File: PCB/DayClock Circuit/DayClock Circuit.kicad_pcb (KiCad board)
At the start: 2 copper layers, 30 x 75 mm, 11 parts, among them J1 Servo Conn_01x03_Male, J2 LED Strip Conn_01x03_Male, J3 5V Power Connector, J4 Input Button Connector, U1 Tiny_RTC_DS1307

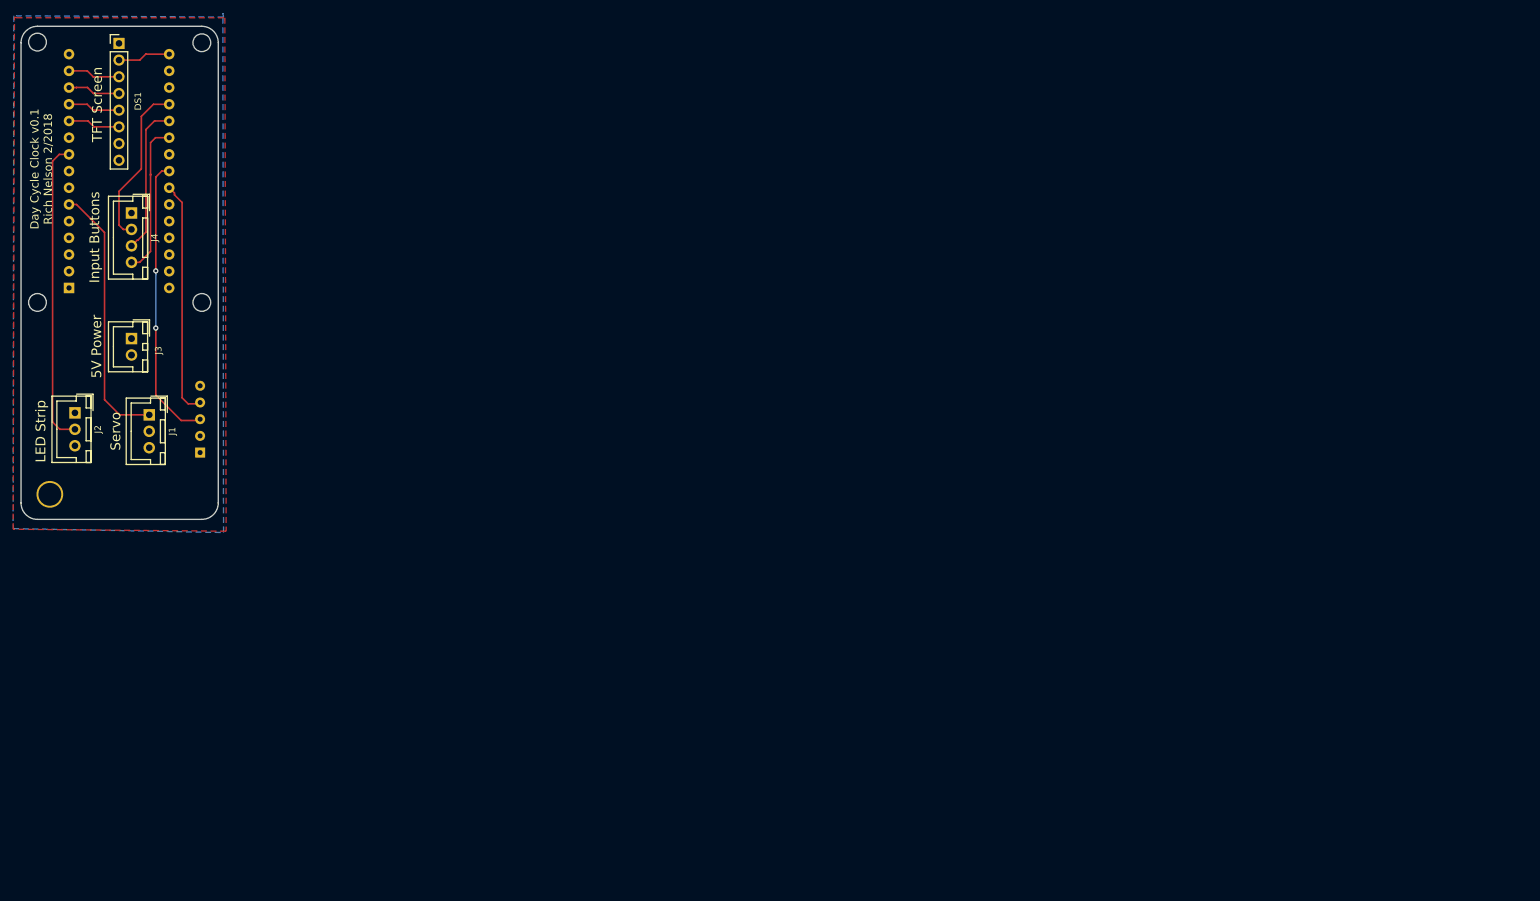
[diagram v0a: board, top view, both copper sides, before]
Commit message: Started moving components to the Arduino Mega,  moved the 3 LED strips (9 PWM pins), and the 32x64 Matrix Display
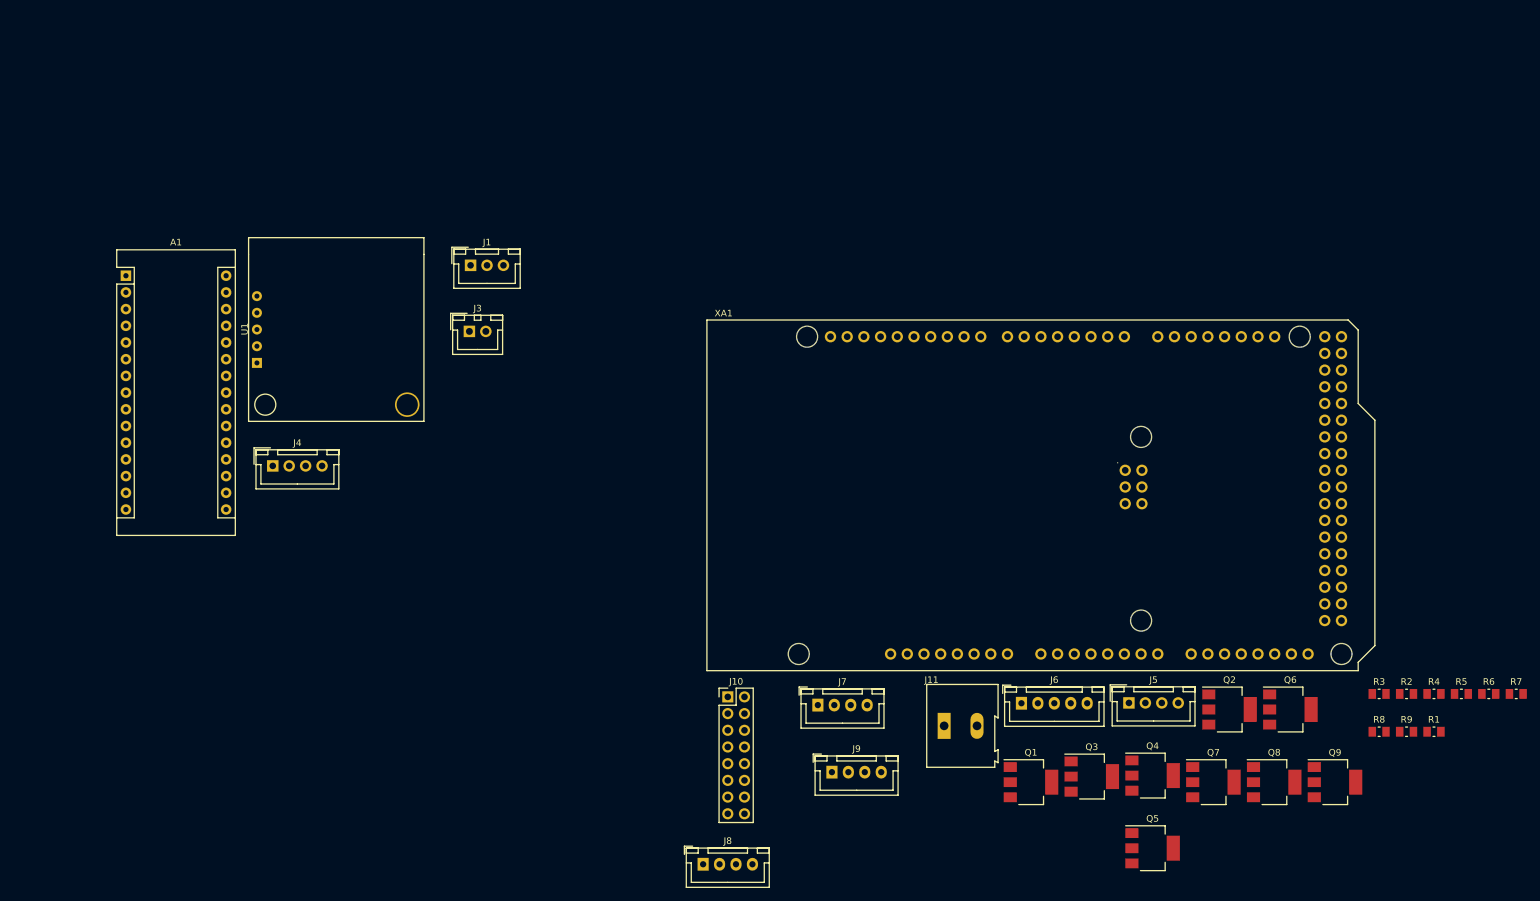
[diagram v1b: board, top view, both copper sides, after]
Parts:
- removed DS1: TFT-Screen-1.44-SPI-128*128, Socket_Strips:Socket_Strip_Straight_1x08_Pitch2.54mm
- removed J2: LED Strip Conn_01x03_Male, Connectors_JST:JST_XH_B03B-XH-A_03x2.50mm_Straight
- removed REF** (x4): MountingHole_2.7mm_M2.5, Mounting_Holes:MountingHole_2.7mm_M2.5
- added J10: Conn_02x08_Odd_Even, Connector_PinHeader_2.54mm:PinHeader_2x08_P2.54mm_Vertical, F.Cu at (107.5, 102.0)
- added J11: Conn_01x02, TerminalBlock:TerminalBlock_Altech_AK300-2_P5.00mm, F.Cu at (140.4, 106.4)
- added J5: 4002 LCD Screen, Connectors_JST:JST_XH_B04B-XH-A_04x2.50mm_Straight, F.Cu at (168.5, 102.9)
- added J6: Encoder, Connector_JST:JST_XH_B05B-XH-A_1x05_P2.50mm_Vertical, F.Cu at (152.2, 103.0)
- added J7: RGB_LED_Strip_Connector, Connector_JST:JST_XH_B04B-XH-A_1x04_P2.50mm_Vertical, F.Cu at (121.2, 103.2)
- added J8: RGB_LED_Strip_Connector, Connector_JST:JST_XH_B04B-XH-A_1x04_P2.50mm_Vertical, F.Cu at (103.7, 127.5)
- added J9: RGB_LED_Strip_Connector, Connector_JST:JST_XH_B04B-XH-A_1x04_P2.50mm_Vertical, F.Cu at (123.3, 113.4)
- added Q1: N-MOSFET, Package_TO_SOT_SMD:SOT-223-3_TabPin2, F.Cu at (153.6, 115.0)
- added Q2: N-MOSFET, Package_TO_SOT_SMD:SOT-223-3_TabPin2, F.Cu at (183.8, 103.9)
- added Q3: N-MOSFET, Package_TO_SOT_SMD:SOT-223-3_TabPin2, F.Cu at (162.9, 114.1)
- added Q4: N-MOSFET, Package_TO_SOT_SMD:SOT-223-3_TabPin2, F.Cu at (172.1, 114.0)
- added Q5: N-MOSFET, Package_TO_SOT_SMD:SOT-223-3_TabPin2, F.Cu at (172.1, 125.0)
- added Q6: N-MOSFET, Package_TO_SOT_SMD:SOT-223-3_TabPin2, F.Cu at (193.1, 103.9)
- added Q7: N-MOSFET, Package_TO_SOT_SMD:SOT-223-3_TabPin2, F.Cu at (181.4, 115.0)
- added Q8: N-MOSFET, Package_TO_SOT_SMD:SOT-223-3_TabPin2, F.Cu at (190.6, 115.0)
- added Q9: N-MOSFET, Package_TO_SOT_SMD:SOT-223-3_TabPin2, F.Cu at (199.9, 115.0)
- added R1: 10k, Resistor_SMD:R_0805_2012Metric_Pad1.15x1.50mm_HandSolder, F.Cu at (214.9, 107.3)
- added R2: 10k, Resistor_SMD:R_0805_2012Metric_Pad1.15x1.50mm_HandSolder, F.Cu at (210.7, 101.5)
- added R3: 10k, Resistor_SMD:R_0805_2012Metric_Pad1.15x1.50mm_HandSolder, F.Cu at (206.6, 101.5)
- added R4: 10k, Resistor_SMD:R_0805_2012Metric_Pad1.15x1.50mm_HandSolder, F.Cu at (214.9, 101.5)
- added R5: 10k, Resistor_SMD:R_0805_2012Metric_Pad1.15x1.50mm_HandSolder, F.Cu at (219.1, 101.5)
- added R6: 10k, Resistor_SMD:R_0805_2012Metric_Pad1.15x1.50mm_HandSolder, F.Cu at (223.3, 101.5)
- added R7: 10k, Resistor_SMD:R_0805_2012Metric_Pad1.15x1.50mm_HandSolder, F.Cu at (227.4, 101.5)
- added R8: 10k, Resistor_SMD:R_0805_2012Metric_Pad1.15x1.50mm_HandSolder, F.Cu at (206.6, 107.3)
- added R9: 10k, Resistor_SMD:R_0805_2012Metric_Pad1.15x1.50mm_HandSolder, F.Cu at (210.7, 107.3)
- added XA1: Arduino_Mega2560_Shield, Arduino:Arduino_Mega2560_Shield, F.Cu at (104.3, 98.0)
- A1, U1: moved to F.Cu
- moved J1 53.9 mm to (68.4, 36.4), turned to 0 degrees
- moved J3 51.4 mm to (68.2, 46.4), turned to 0 degrees
- moved J4 44.1 mm to (38.3, 66.9), turned to 0 degrees
- moved U1 19.3 mm to (38.4, 61.4), turned to 0 degrees
- moved A1 8.85 mm to (16.0, 37.9)
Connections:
- net /RTC_SCL renamed /SCL
- net /RTC_SDA renamed /SDA
- A1 pad 11: /TFT_CS -> (no net)
- A1 pad 12: /TFT_RST -> (no net)
- A1 pad 13: /TFT_A0 -> (no net)
- A1 pad 14: /TFT_SDA -> (no net)
- A1 pad 16: /TFT_SCK -> (no net)
- A1 pad 22: (no net) -> /ENC_SW
- A1 pad 5: (no net) -> /ENC_DT
- A1 pad 7: (no net) -> /ENC_CLK
- A1 pad 9: /LED_DATA -> (no net)
- J4 pad 1: GND -> (no net)
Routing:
- net /LED_DATA: track 46.5 -> 0.00 mm
- net /SDA: track 43.5 -> 0.00 mm, vias 2 -> 0
- net /SVO_DATA: track 40.3 -> 0.00 mm
- net /SCL: track 35.6 -> 0.00 mm
- net /BTN_3: track 25.1 -> 0.00 mm
- net /BTN_1: track 23.5 -> 0.00 mm
- net /BTN_2: track 22.7 -> 0.00 mm
- net /TFT_SCK: track 8.05 -> 0.00 mm
- net /TFT_SDA: track 7.99 -> 0.00 mm
- net /TFT_A0: track 7.99 -> 0.00 mm
- net /TFT_RST: track 7.97 -> 0.00 mm
- net /TFT_CS: track 7.97 -> 0.00 mm
- removed copper zone on F.Cu, net +5V
- removed copper zone on B.Cu, net GND
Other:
- board outline removed
- board text removed: "5V Power"
- board text removed: "Arduino Nano"
- board text removed: "Day Cycle Clock v0.1 Rich Nelson 2/2018"
- board text removed: "Input Buttons"
- board text removed: "LED Strip"
- board text removed: "RTCTiny"
- board text removed: "Servo"
- board text removed: "TFT Screen"

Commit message: Added Stepper with Driver and Proximity Sensor Limits
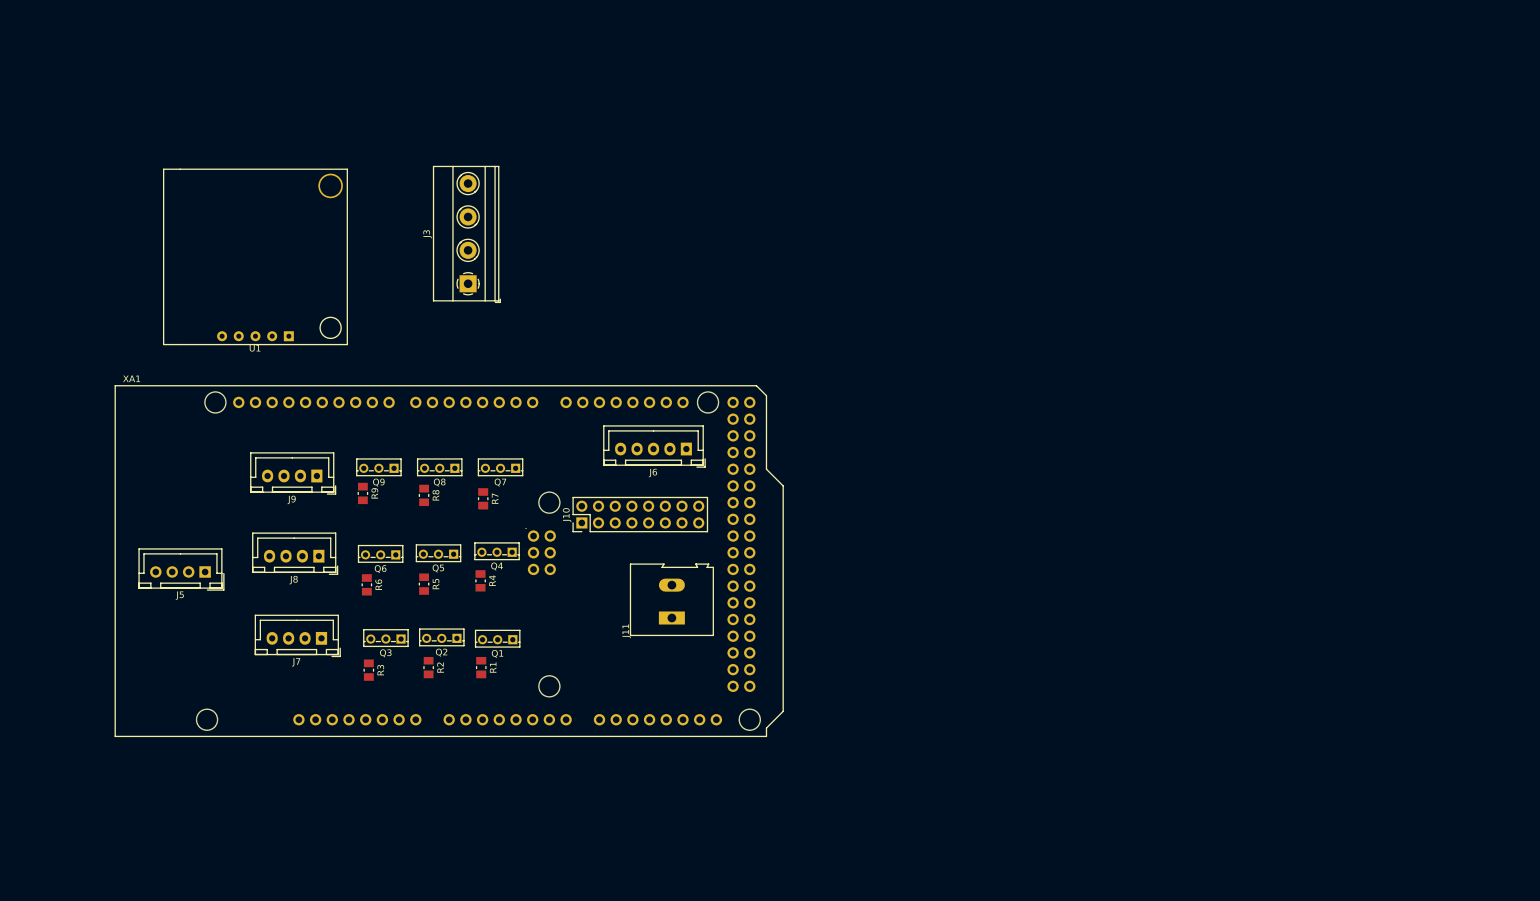
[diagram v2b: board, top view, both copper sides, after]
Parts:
- removed A1: Arduino_Nano_v3.x, Modules:Arduino_Nano
- removed J1: Servo Conn_01x03_Male, Connectors_JST:JST_XH_B03B-XH-A_03x2.50mm_Straight
- removed J4: Input Button Connector, Connectors_JST:JST_XH_B04B-XH-A_04x2.50mm_Straight
- J3: value 5V Power Connector -> molex 15-24-4441; footprint Connectors_JST:JST_XH_B02B-XH-A_02x2.50mm_Straight -> TerminalBlock_Phoenix:TerminalBlock_Phoenix_MKDS-1,5-4-5.08_1x04_P5.08mm_Horizontal
- Q1, Q2, Q3, Q4, Q5, Q6, Q7, Q8, Q9: footprint Package_TO_SOT_SMD:SOT-223-3_TabPin2 -> Package_TO_SOT_THT:TO-251_IPAK_Vertical
- moved R6 171.5 mm to (52.6, 85.0), turned to 270 degrees
- moved R9 162.8 mm to (52.0, 71.1), turned to 270 degrees
- moved R7 159.9 mm to (70.3, 71.9), turned to 270 degrees
- moved R5 158.7 mm to (61.3, 84.8), turned to 270 degrees
- moved R3 153.7 mm to (52.9, 97.9), turned to 270 degrees
- moved Q9 150.9 mm to (56.7, 67.2), turned to 180 degrees
- moved R8 149.7 mm to (61.3, 71.4), turned to 270 degrees
- moved R2 148.8 mm to (62.0, 97.5), turned to 270 degrees
- moved R4 146.0 mm to (69.9, 84.4), turned to 270 degrees
- moved R1 145.2 mm to (70.0, 97.5), turned to 270 degrees
- moved J5 141.9 mm to (28.0, 83.0), turned to 180 degrees
- moved Q6 138.1 mm to (57.0, 80.4), turned to 180 degrees
- moved Q8 133.5 mm to (66.0, 67.2), turned to 180 degrees
- moved Q2 118.0 mm to (66.3, 93.1), turned to 180 degrees
- moved Q7 116.4 mm to (75.2, 67.2), turned to 180 degrees
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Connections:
- J10 pad 1: (no net) -> /D24
- J10 pad 11: (no net) -> /A2
- J10 pad 13: (no net) -> /D13
- J10 pad 15: (no net) -> /D31
- J10 pad 3: (no net) -> /D26
- J10 pad 5: (no net) -> /D27
- J10 pad 7: (no net) -> /D29
- J10 pad 9: (no net) -> /A0
- J3 pad 1: +5V -> +12V
- J6 pad 3: /ENC_SW -> /D19
- J6 pad 4: /ENC_DT -> /D18
- J6 pad 5: /ENC_CLK -> /D17
- XA1 pad A0: (no net) -> /A0
- XA1 pad A2: (no net) -> /A2
- XA1 pad D13: (no net) -> /D13
- XA1 pad D17: (no net) -> /D17
- XA1 pad D18: (no net) -> /D18
- XA1 pad D19: (no net) -> /D19
- XA1 pad D24: (no net) -> /D24
- XA1 pad D26: (no net) -> /D26
- XA1 pad D27: (no net) -> /D27
- XA1 pad D29: (no net) -> /D29
- XA1 pad D31: (no net) -> /D31
- XA1 pad SCL: (no net) -> /SCL
- XA1 pad SDA: (no net) -> /SDA
